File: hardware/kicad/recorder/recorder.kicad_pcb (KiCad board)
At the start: 4 copper layers, 64 x 86 mm, 60 parts, among them J1 UART0, J2 USB_C_16P, J3 microSD, SW1 record, U1 ESP32-S3-MINI-1U-N8, U2 ES8311, U3 MCP73831-2-OT, U4 AP2112K-3.3, U5 AP22804AW5, U6 NS4150B, U7 USBLC6-2SC6, U8 LP5907MFX-3.3, Y1 12.288MHz

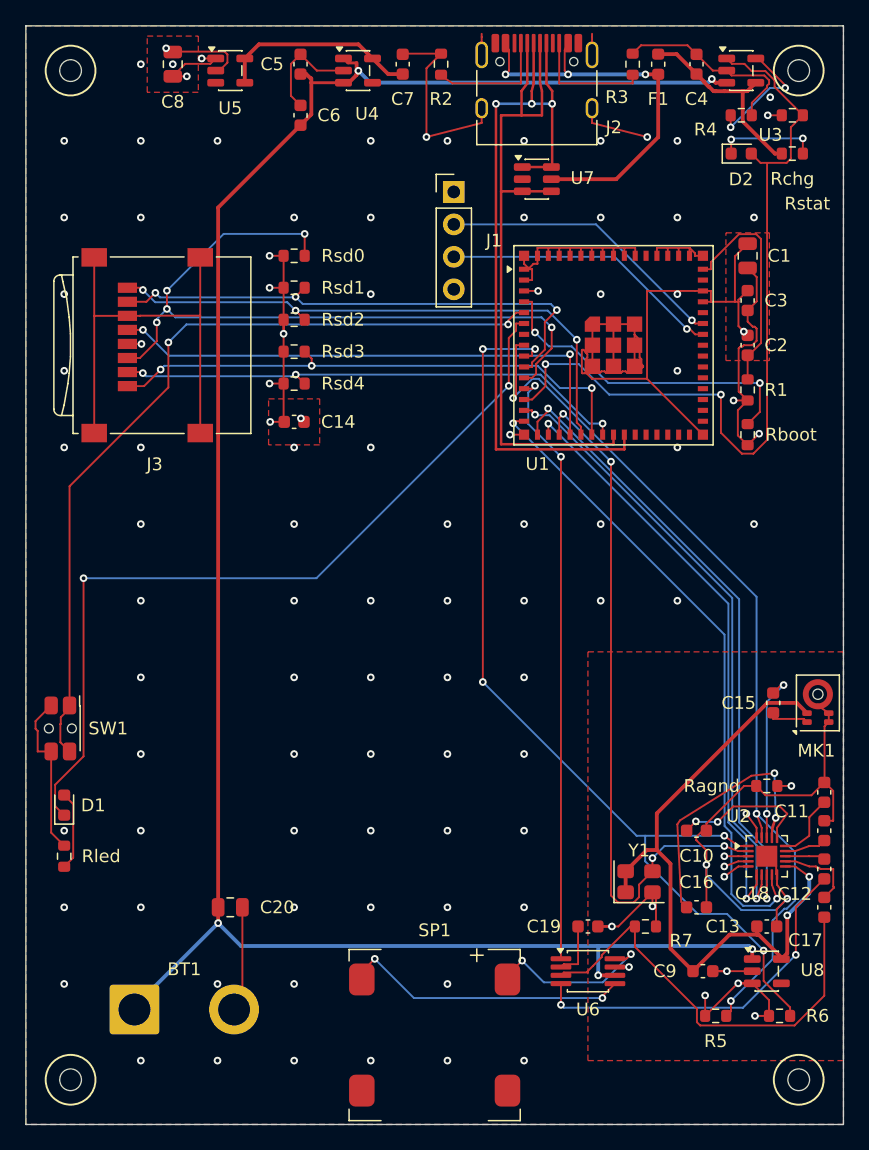
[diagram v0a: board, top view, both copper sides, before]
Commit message: Swap in a BQ24074 power-path charger so USB can run the board with the pouch unplugged.
Co-authored-by: Cursor <cursoragent@cursor.com>
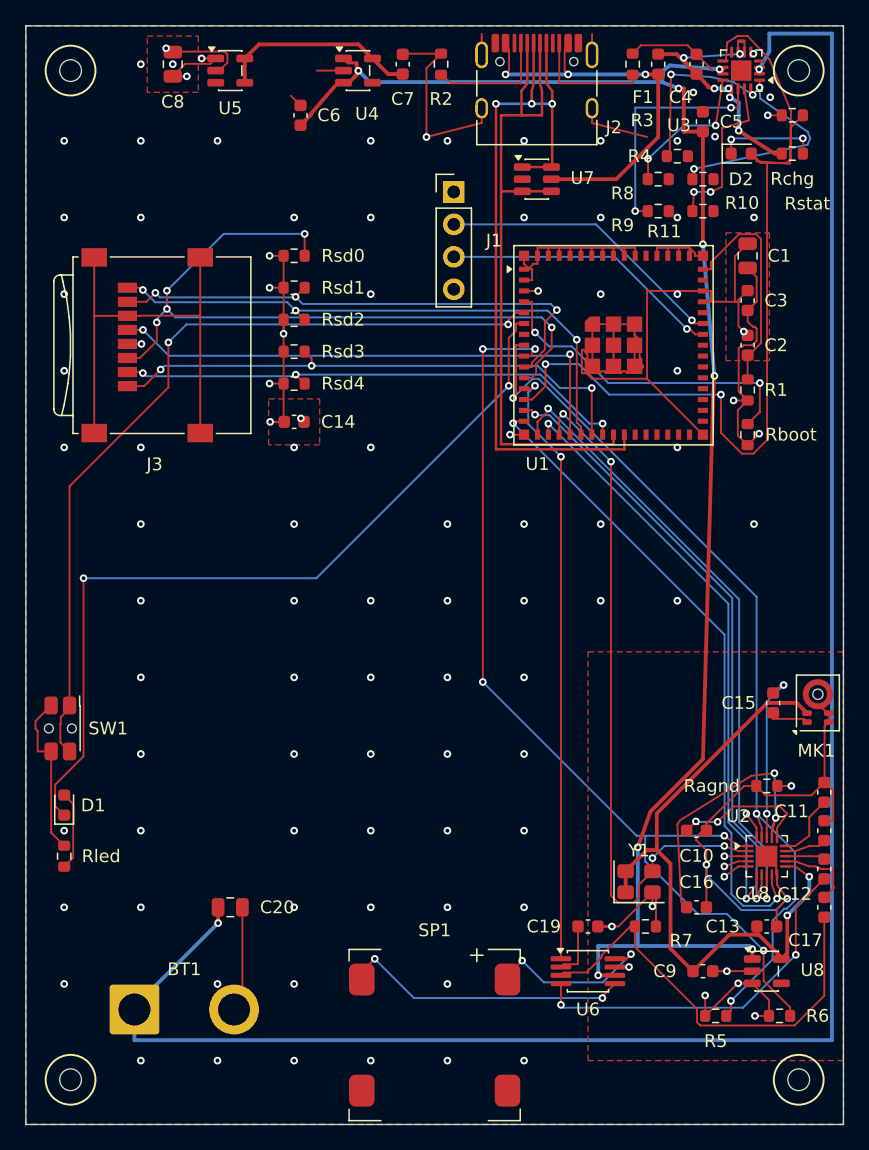
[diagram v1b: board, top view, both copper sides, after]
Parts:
- added R10: 10k, Resistor_SMD:R_0603_1608Metric, F.Cu at (21.0, -31.0)
- added R11: 3.01k, Resistor_SMD:R_0603_1608Metric, F.Cu at (21.0, -28.5)
- added R8: 3.01k, Resistor_SMD:R_0603_1608Metric, F.Cu at (17.5, -31.0)
- added R9: 49.9k, Resistor_SMD:R_0603_1608Metric, F.Cu at (17.5, -28.5)
- BT1: value LiPo 500mAh -> JST-PH 1S
- R4: value 2k -> 1.8k
- U3: value MCP73831-2-OT -> BQ24074RGTR; footprint Package_TO_SOT_SMD:SOT-23-5 -> Package_DFN_QFN:VQFN-16-1EP_3x3mm_P0.5mm_EP1.6x1.6mm
- moved C5 31.8 mm to (21.0, -35.5)
- moved R4 5.94 mm to (19.0, -32.8)
- turned U3 to 180 degrees
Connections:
- C5 pad 1: VBAT -> VSYS
- C6 pad 1: VBAT -> VSYS
- R4 pad 1: /Power/PROG -> /Power/ISET
- U3 pad 1: CHG_STAT -> /Power/TS
- U3 pad 2: GND -> VBAT
- U3 pad 4: VBUS_CHG -> GND
- U3 pad 5: /Power/PROG -> GND
- U4 pad 1: VBAT -> VSYS
- U4 pad 3: VBAT -> VSYS
- U6 pad 6: VBAT -> VSYS
- U8 pad 1: VBAT -> VSYS
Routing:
- net VSYS: track 0.00 -> 126.9 mm, vias 0 -> 8
- net /Power/TMR: track 0.00 -> 18.6 mm, vias 0 -> 2
- net /Power/TS: track 0.00 -> 16.6 mm, vias 0 -> 2
- net GND: track 217.9 -> 204.5 mm, vias 86 -> 88
- net /Power/ITERM: track 0.00 -> 13.1 mm, vias 0 -> 2
- net /Power/ISET: track 0.00 -> 12.9 mm, vias 0 -> 2
- net /Power/ILIM: track 0.00 -> 11.5 mm, vias 0 -> 2
- net /Power/PROG: track 9.87 -> 0.00 mm, vias 2 -> 0
- net CHG_STAT: track 63.4 -> 72.3 mm
- net VBUS_CHG: track 15.6 -> 22.4 mm, vias 0 -> 6
- net VBAT: track 162.2 -> 155.4 mm, vias 5 -> 2

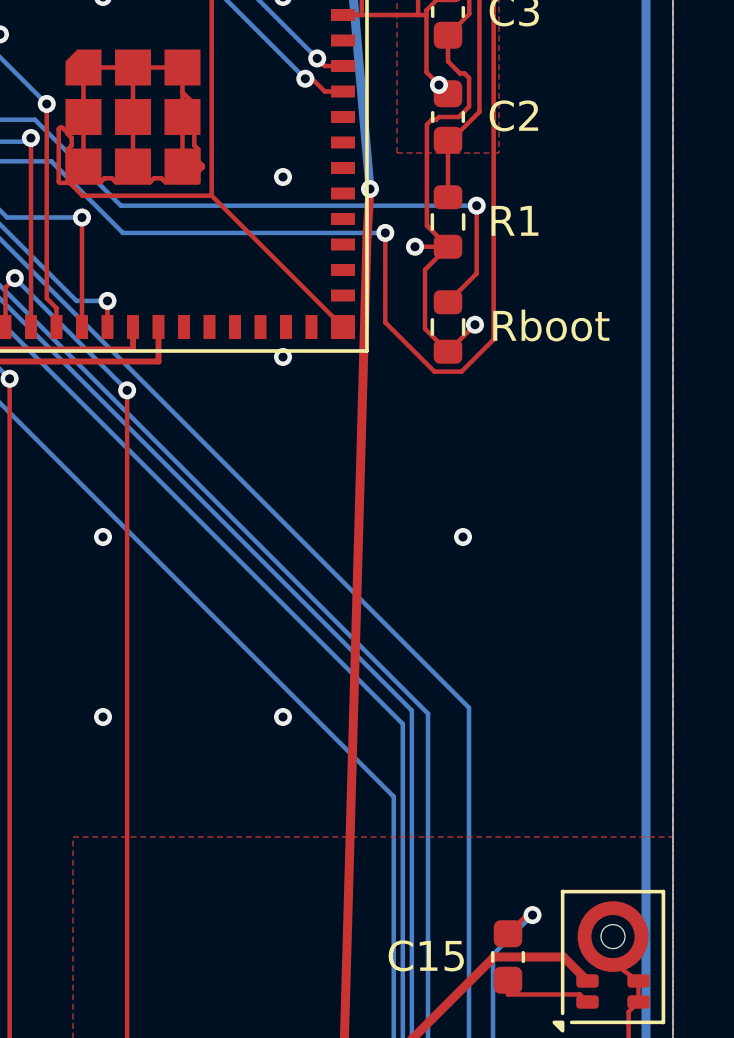
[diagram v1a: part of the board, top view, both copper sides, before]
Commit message: Add SMT Boot and Reset buttons so the board can enter download mode after USB mass-storage owns the port.
Co-authored-by: Cursor <cursoragent@cursor.com>
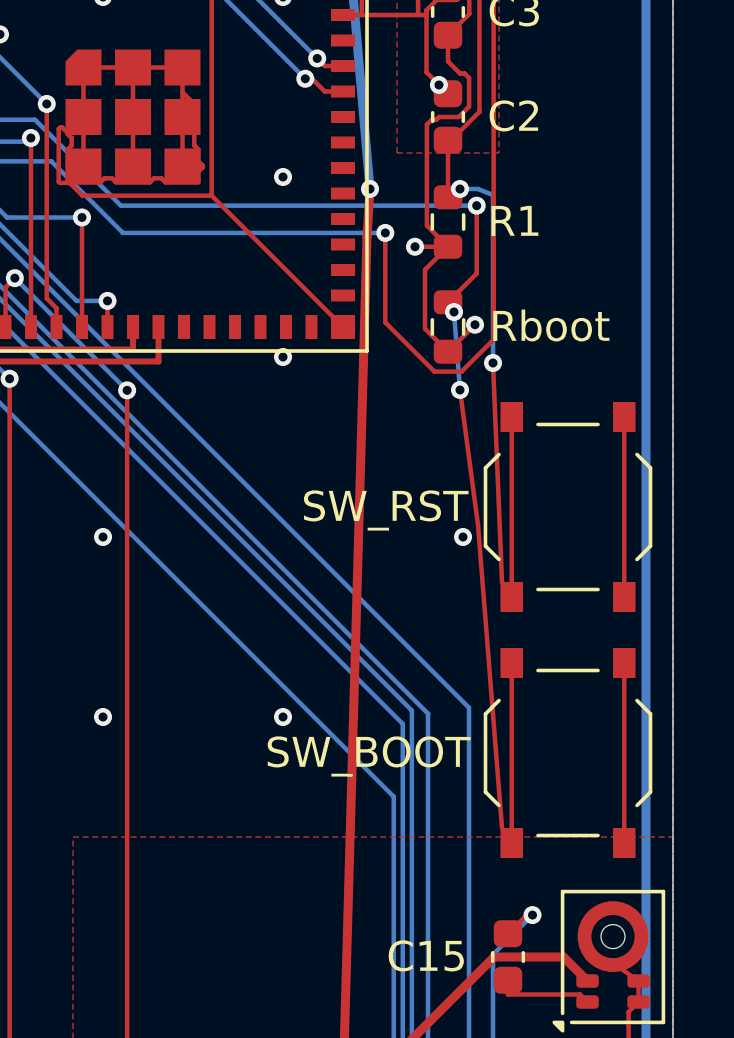
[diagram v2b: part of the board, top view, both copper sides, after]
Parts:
- added SW_BOOT: boot, Button_Switch_SMD:SW_Push_1P1T_XKB_TS-1187A, F.Cu at (28.5, 3.20)
- added SW_RST: reset, Button_Switch_SMD:SW_Push_1P1T_XKB_TS-1187A, F.Cu at (28.5, -5.00)
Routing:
- net /MCU_USB/BOOT: track 26.0 -> 49.3 mm, vias 2 -> 4
- net /MCU_USB/EN: track 17.7 -> 37.7 mm, vias 0 -> 2
- net GND: track 204.5 -> 216.5 mm

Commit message: Put the real JST-PH on BT1, add a BAT ceramic at U3, and document lid-off Boot/Reset.
The power-path PR still shipped a 7.8 mm solder-wire land while the BOM
named S2B-PH-K-S. Owner chose the real 2.00 mm connector: pad 1 stays at
(-23.5, 34) on VBAT so the existing B.Cu hop still hits it, pad 2 moves
to (-21.5, 34) on GND. C21 is 10 µF next to U3 BAT for USB with the pouch
unplugged. The 6.0 mm housing does not fit the 5.45 mm lid cavity, so the
case cuts a window through shell_back. Boot and Reset stay lid-off; a
flush hole would not reach the 5 mm actuators. power_path.cir now runs
USB-with-BT1-open and pouch-only through a BATFET.

Co-authored-by: Cursor <cursoragent@cursor.com>
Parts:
- added C21: 10uF, Capacitor_SMD:C_0603_1608Metric, F.Cu at (30.8, -26.5)
- BT1: footprint Connector_Wire:SolderWire-2sqmm_1x02_P7.8mm_D2mm_OD3.9mm -> Connector_JST:JST_PH_S2B-PH-K_1x02_P2.00mm_Horizontal
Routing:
- net VBAT: track 155.4 -> 168.8 mm, vias 2 -> 4
- net GND: track 216.5 -> 208.3 mm, vias 88 -> 87
